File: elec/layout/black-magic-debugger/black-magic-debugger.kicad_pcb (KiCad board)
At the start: 2 copper layers, 24 parts

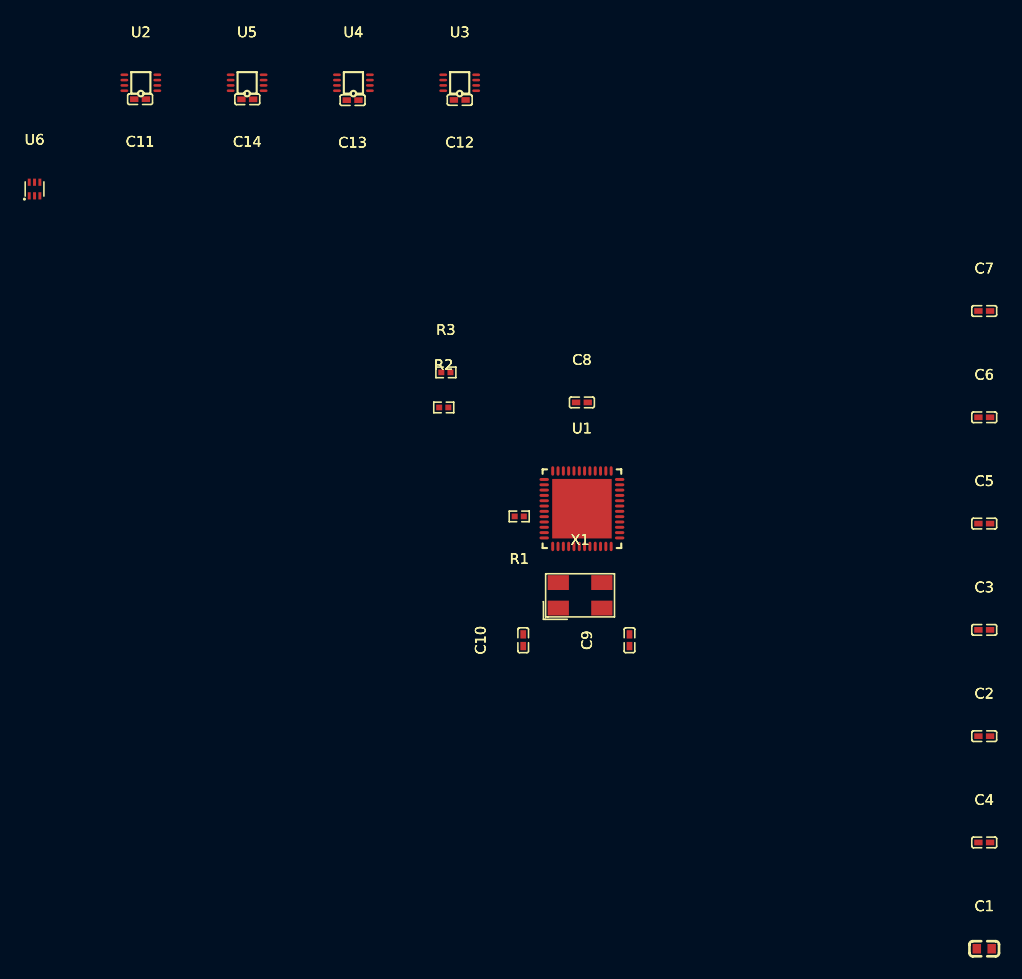
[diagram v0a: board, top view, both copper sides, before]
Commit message: add SWD header, finished routing
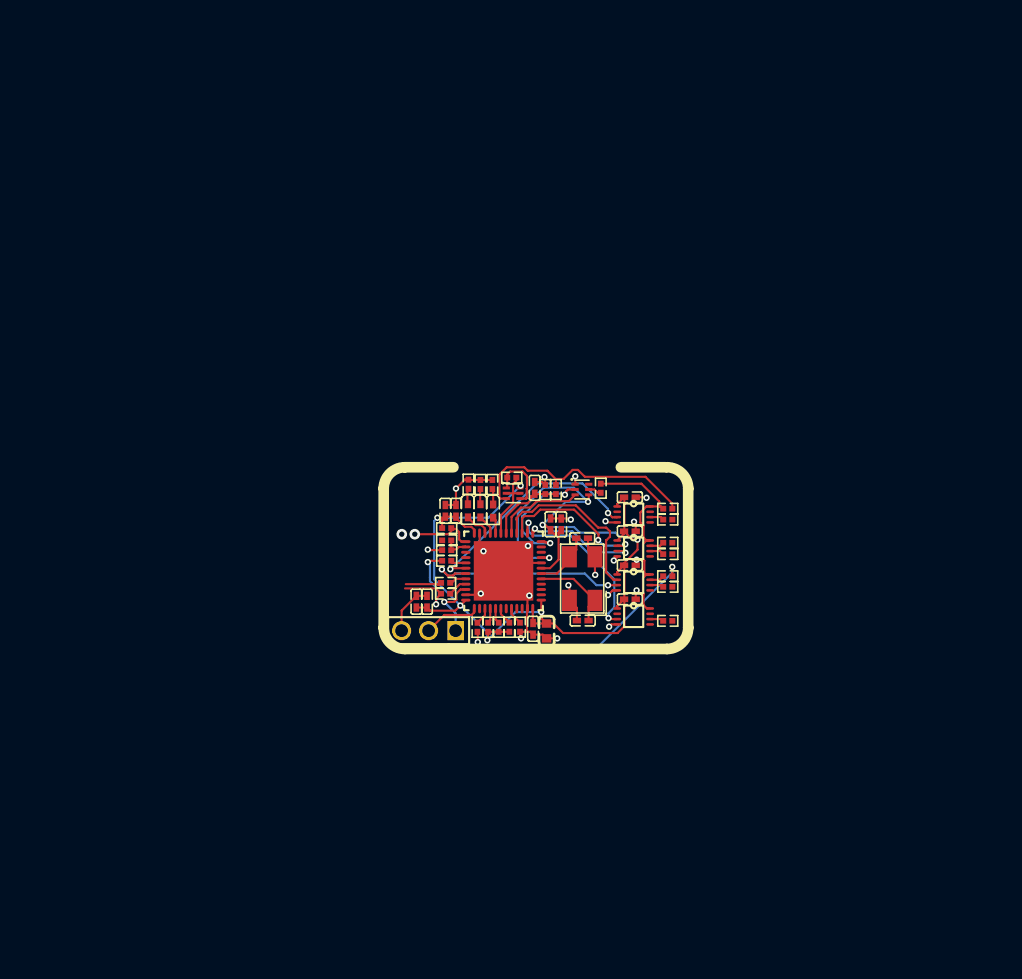
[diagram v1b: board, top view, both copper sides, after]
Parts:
- added C15: 100nF ±10% 16V X7R, atopile:C0402-b3ef17, F.Cu at (117.5, 51.4)
- added D1: , atopile:LED0402-R-RD-049f90, F.Cu at (113.6, 53.6)
- added D2: , atopile:LED0402-R-RD-049f90, F.Cu at (112.4, 53.6)
- added D3: , atopile:LED0402-R-RD-049f90, F.Cu at (111.2, 53.6)
- added P1: , atopile:HDR-TH_3P-P2.54-V-M-1-04b1f3, F.Cu at (107.5, 64.8)
- added R10: 1.5kΩ ±1% 62.5mW, atopile:R0402-56259e, F.Cu at (109.2, 58.3)
- added R11: 10kΩ ±1% 62.5mW, atopile:R0402-56259e, F.Cu at (109.2, 55.2)
- added R12: 10kΩ ±1% 62.5mW, atopile:R0402-56259e, F.Cu at (115.3, 50.5)
- added R13: 10kΩ ±1% 62.5mW, atopile:R0402-56259e, F.Cu at (123.7, 51.5)
- added R14: 100Ω ±1% 62.5mW, atopile:R0402-56259e, F.Cu at (130.0, 56.6)
- added R15: 100Ω ±1% 62.5mW, atopile:R0402-56259e, F.Cu at (130.0, 57.6)
- added R16: 100Ω ±1% 62.5mW, atopile:R0402-56259e, F.Cu at (130.0, 59.7)
- added R17: 100Ω ±1% 62.5mW, atopile:R0402-56259e, F.Cu at (130.0, 63.9)
- added R18: 100Ω ±1% 62.5mW, atopile:R0402-56259e, F.Cu at (112.1, 64.5)
- added R20: 10kΩ ±1% 62.5mW, atopile:R0402-56259e, F.Cu at (109.2, 57.3)
- added R21: 4.7kΩ ±1% 62.5mW, atopile:R0402-56259e, F.Cu at (109.2, 56.4)
- added R22: 10kΩ ±1% 62.5mW, atopile:R0402-56259e, F.Cu at (118.5, 51.6)
- added R23: 4.7kΩ ±1% 62.5mW, atopile:R0402-56259e, F.Cu at (119.5, 51.6)
- added R24: 100Ω ±1% 62.5mW, atopile:R0402-56259e, F.Cu at (130.0, 53.4)
- added R25: 100Ω ±1% 62.5mW, atopile:R0402-56259e, F.Cu at (130.0, 60.7)
- added R26: 100Ω ±1% 62.5mW, atopile:R0402-56259e, F.Cu at (130.0, 54.4)
- added R4: 10kΩ ±1% 62.5mW, atopile:R0402-56259e, F.Cu at (113.1, 64.5)
- added R5: 10kΩ ±1% 62.5mW, atopile:R0402-56259e, F.Cu at (114.1, 64.5)
- added R6: 10kΩ ±1% 62.5mW, atopile:R0402-56259e, F.Cu at (115.1, 64.5)
- added R7: 1kΩ ±1% 62.5mW, atopile:R0402-56259e, F.Cu at (113.5, 51.1)
- added R8: 1kΩ ±1% 62.5mW, atopile:R0402-56259e, F.Cu at (112.4, 51.1)
- added R9: 1kΩ ±1% 62.5mW, atopile:R0402-56259e, F.Cu at (111.3, 51.1)
- added U7: , atopile:SOT-563-6_L1.6-W1.2-P0.5-LS1.6-BL-d9216f, F.Cu at (121.9, 51.6)
- moved U5 62.0 mm to (126.8, 63.5), turned to 180 degrees
- moved U2 61.6 mm to (126.8, 53.9), turned to 180 degrees
- moved C11 59.4 mm to (126.5, 52.3), turned to 0 degrees
- moved C14 59.2 mm to (126.5, 61.9), turned to 0 degrees
- moved C4 57.1 mm to (107.4, 62.1), turned to 90 degrees
- moved C2 54.9 mm to (106.4, 62.1), turned to 90 degrees
- moved C7 54.1 mm to (109.1, 53.6), turned to 90 degrees
- moved U4 53.9 mm to (126.8, 60.3), turned to 180 degrees
- moved U6 53.4 mm to (115.5, 51.9), turned to -90 degrees
- moved C1 50.9 mm to (118.6, 64.9), turned to -90 degrees
- moved C5 49.7 mm to (110.1, 53.6), turned to 90 degrees
- moved C13 48.2 mm to (126.5, 55.5), turned to 0 degrees
- moved U3 46.8 mm to (126.8, 57.1), turned to 180 degrees
- moved C12 46.6 mm to (126.5, 58.7), turned to 0 degrees
- moved C3 42.5 mm to (117.3, 64.7), turned to -90 degrees
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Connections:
- net level_shifter_1-A1 renamed lvl_shifter_1-A1
- net level_shifter_1-B1 renamed lvl_shifter_1-B1
- net level_shifter_1-DIR renamed lvl_shifter_1-DIR
- net level_shifter_2-DIR renamed lvl_shifter_2-DIR
- net level_shifter_3-DIR renamed lvl_shifter_3-DIR
- net level_shifter_4-A1 renamed lvl_shifter_4-A1
- net level_shifter_4-B1 renamed lvl_shifter_4-B1
- net level_shifter_4-DIR renamed lvl_shifter_4-DIR
- C1 pad 1: hv-3 -> hv
- C10 pad 2: gnd-3 -> gnd
- C11 pad 1: hv-4 -> hv
- C11 pad 2: gnd-4 -> gnd
- C12 pad 1: hv-1 -> hv
- C12 pad 2: gnd-5 -> gnd
- C13 pad 1: hv-2 -> hv
- C13 pad 2: gnd-2 -> gnd
- C14 pad 2: gnd-1 -> gnd
- C2 pad 1: hv-3 -> hv
- C3 pad 1: hv-3 -> hv
- C4 pad 1: hv-3 -> hv
- C5 pad 1: hv-3 -> hv
- C6 pad 1: hv-3 -> hv
- C7 pad 1: hv-3 -> hv
- C9 pad 2: gnd-3 -> gnd
- U1 pad 1: hv-3 -> hv
- U1 pad 12: PA2 -> G2
- U1 pad 13: PA3 -> line-9
- U1 pad 14: PA4 -> line
- U1 pad 15: PA5 -> line-13
- U1 pad 16: PA6 -> line-7
- U1 pad 17: PA7 -> D1
- U1 pad 18: PB0 -> line-6
- U1 pad 19: PB1 -> G2-1
- U1 pad 20: PB2 -> anode
- U1 pad 21: PB10 -> anode-1
- U1 pad 22: PB11 -> anode-2
- U1 pad 24: hv-3 -> hv
- U1 pad 26: PB13 -> line-10
- U1 pad 30: PA9 -> line-12
- U1 pad 31: PA10 -> line-3
- U1 pad 36: hv-3 -> hv
- U1 pad 48: hv-3 -> hv
- U1 pad 49: EP -> gnd
- U1 pad 9: hv-3 -> hv
- U2 pad 1: hv-4 -> hv
- U2 pad 3: level_shifter_1-A2 -> line-12
- U2 pad 4: gnd-4 -> gnd
- U2 pad 6: level_shifter_1-B2 -> B2-2
- U2 pad 8: level_shifter_1-VCCB -> VCCB
- U3 pad 1: hv-1 -> hv
- U3 pad 2: level_shifter_2-A1 -> line-13
- U3 pad 3: level_shifter_2-A2 -> line-9
- U3 pad 4: gnd-5 -> gnd
- U3 pad 6: level_shifter_2-B2 -> B2
- U3 pad 7: level_shifter_2-B1 -> B1-1
- U3 pad 8: level_shifter_2-VCCB -> VCCB
- U4 pad 1: hv-2 -> hv
- U4 pad 2: level_shifter_3-A1 -> line-7
- U4 pad 3: level_shifter_3-A2 -> line-3
- U4 pad 4: gnd-2 -> gnd
- U4 pad 6: level_shifter_3-B2 -> B2-1
- U4 pad 7: level_shifter_3-B1 -> B1
- U4 pad 8: level_shifter_3-VCCB -> VCCB
- U5 pad 3: level_shifter_4-A2 -> line
- U5 pad 4: gnd-1 -> gnd
- U5 pad 6: level_shifter_4-B2 -> B2-3
- U5 pad 8: level_shifter_4-VCCB -> VCCB
- U6 pad 1: S2 -> S1
- U6 pad 2: G2 -> G2-1
- U6 pad 3: D1 -> hv-2
- U6 pad 5: G1 -> G2-1
- U6 pad 6: D2 -> hv
- X1 pad 2: gnd-3 -> gnd
- X1 pad 4: gnd-3 -> gnd
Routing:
- net hv: track 0.00 -> 106.5 mm, vias 0 -> 9
- net gnd: track 0.00 -> 61.6 mm, vias 0 -> 22
- net line-1: track 0.00 -> 23.7 mm, vias 0 -> 2
- net hv-2: track 0.00 -> 22.7 mm
- net line-12: track 0.00 -> 22.2 mm, vias 0 -> 2
- net VCCB: track 0.00 -> 20.7 mm
- net line-3: track 0.00 -> 19.9 mm, vias 0 -> 2
- net line-7: track 0.00 -> 17.1 mm
- net line: track 0.00 -> 16.5 mm, vias 0 -> 2
- net line-13: track 0.00 -> 14.1 mm, vias 0 -> 2
- net G2: track 0.00 -> 11.6 mm, vias 0 -> 2
- net line-9: track 0.00 -> 10.8 mm, vias 0 -> 2
- net micro-line-1: track 0.00 -> 10.5 mm, vias 0 -> 2
- net D1: track 0.00 -> 8.37 mm
- net xin: track 0.00 -> 8.04 mm
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
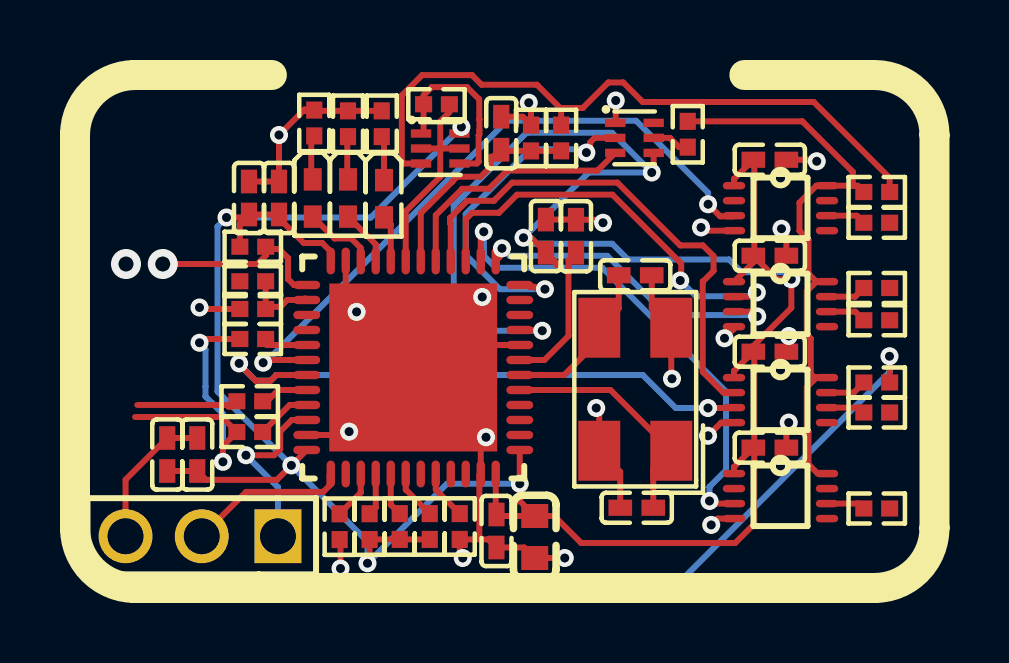
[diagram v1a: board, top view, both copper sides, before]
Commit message: Correct DIR pins
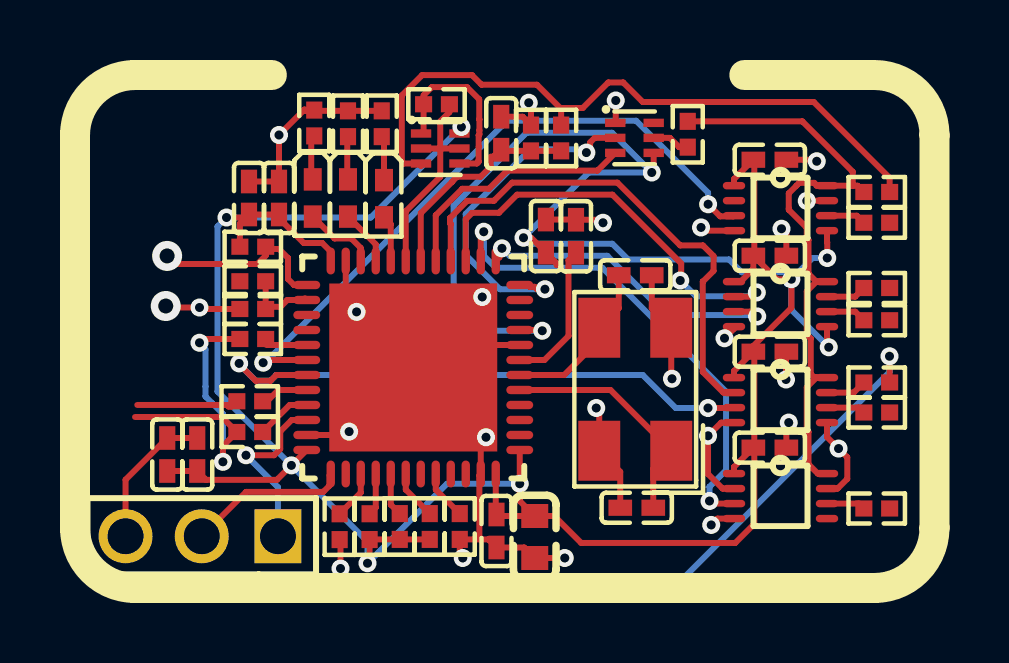
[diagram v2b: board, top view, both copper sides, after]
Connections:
- net lvl_shifter_4-DIR renamed DIR
- C15 pad 1: line-6 -> line-5
- R10 pad 1: micro-line-1 -> line-4
- R12 pad 1: G2-1 -> G1
- R13 pad 2: G1 -> G1-1
- R14 pad 2: line-2 -> line-13
- R15 pad 2: line-11 -> line-3
- R16 pad 2: line-1 -> line-2
- R17 pad 1: B2-3 -> B2-2
- R17 pad 2: line-4 -> line
- R18 pad 2: line-1 -> line-2
- R2 pad 1: micro-line -> line-9
- R20 pad 1: line-10 -> line-11
- R21 pad 1: hv-1 -> hv-2
- R21 pad 2: line-10 -> line-11
- R22 pad 1: line-6 -> line-5
- R23 pad 1: hv-2 -> hv-1
- R23 pad 2: line-6 -> line-5
- R24 pad 2: hv-2 -> hv-1
- R25 pad 1: B2-1 -> B2-3
- R25 pad 2: line-8 -> line-15
- R26 pad 1: B2-2 -> B2-1
- R26 pad 2: line-5 -> line-6
- R3 pad 1: micro-line-1 -> line-4
- U1 pad 13: line-9 -> line-1
- U1 pad 14: line -> line-7
- U1 pad 15: line-13 -> line-14
- U1 pad 16: line-7 -> line-12
- U1 pad 18: line-6 -> line-5
- U1 pad 19: G2-1 -> G1
- U1 pad 26: line-10 -> line-11
- U1 pad 30: line-12 -> line-10
- U1 pad 31: line-3 -> line-8
- U2 pad 2: lvl_shifter_1-A1 -> gnd
- U2 pad 3: line-12 -> line-10
- U2 pad 5: lvl_shifter_1-DIR -> hv
- U2 pad 6: B2-2 -> B2-1
- U2 pad 7: lvl_shifter_1-B1 -> gnd
- U3 pad 2: line-13 -> line-14
- U3 pad 3: line-9 -> line-1
- U3 pad 5: lvl_shifter_2-DIR -> hv
- U4 pad 2: line-7 -> line-12
- U4 pad 3: line-3 -> line-8
- U4 pad 5: lvl_shifter_3-DIR -> gnd
- U4 pad 6: B2-1 -> B2-3
- U5 pad 2: lvl_shifter_4-A1 -> gnd
- U5 pad 3: line -> line-7
- U5 pad 6: B2-3 -> B2-2
- U5 pad 7: lvl_shifter_4-B1 -> gnd
- U6 pad 2: G2-1 -> G1
- U6 pad 3: hv-2 -> hv-1
- U6 pad 5: G2-1 -> G1
- U7 pad 5: G1 -> G1-1
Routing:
- net line-2: track 0.00 -> 23.7 mm, vias 0 -> 2
- net hv-2: track 22.7 -> 0.00 mm
- net hv-1: track 0.00 -> 22.7 mm
- net line-8: track 0.00 -> 19.9 mm, vias 0 -> 2
- net line-3: track 19.9 -> 0.00 mm, vias 2 -> 0
- net line-10: track 2.58 -> 22.2 mm, vias 0 -> 2
- net line: track 16.5 -> 0.00 mm, vias 2 -> 0
- net line-14: track 0.00 -> 14.1 mm, vias 0 -> 2
- net line-13: track 14.1 -> 0.00 mm, vias 2 -> 0
- net line-1: track 23.7 -> 10.8 mm
- net micro-line-1: track 10.5 -> 0.00 mm, vias 2 -> 0
- net line-4: track 0.00 -> 10.5 mm, vias 0 -> 2
- net gnd: track 61.6 -> 69.1 mm, vias 22 -> 24
- net line-9: track 10.8 -> 3.41 mm, vias 2 -> 0
- net line-6: track 7.33 -> 0.00 mm
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
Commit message: Build everything with ordered params to fix frozen builds
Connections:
- net S1 renamed S2
- C1 pad 1: hv -> hv-2
- C11 pad 1: hv -> hv-2
- C12 pad 1: hv -> hv-2
- C13 pad 1: hv -> hv-2
- C14 pad 1: hv -> hv-2
- C15 pad 1: line-5 -> line-12
- C2 pad 1: hv -> hv-2
- C3 pad 1: hv -> hv-2
- C4 pad 1: hv -> hv-2
- C5 pad 1: hv -> hv-2
- C6 pad 1: hv -> hv-2
- C7 pad 1: hv -> hv-2
- D1 pad 1: anode -> anode-2
- D3 pad 1: anode-2 -> anode
- R10 pad 1: line-4 -> line-6
- R11 pad 2: hv -> hv-2
- R12 pad 1: G1 -> G1-1
- R13 pad 2: G1-1 -> G1
- R14 pad 2: line-13 -> line-4
- R15 pad 1: B2 -> B2-1
- R15 pad 2: line-3 -> line-13
- R16 pad 2: line-2 -> line-7
- R17 pad 2: line -> line-11
- R18 pad 2: line-2 -> line-7
- R2 pad 1: line-9 -> line-15
- R20 pad 1: line-11 -> line-1
- R21 pad 1: hv-2 -> hv-1
- R21 pad 2: line-11 -> line-1
- R22 pad 1: line-5 -> line-12
- R23 pad 1: hv-1 -> hv
- R23 pad 2: line-5 -> line-12
- R24 pad 2: hv-1 -> hv
- R25 pad 1: B2-3 -> B2
- R25 pad 2: line-15 -> line-3
- R26 pad 1: B2-1 -> B2-3
- R26 pad 2: line-6 -> line-8
- R3 pad 1: line-4 -> line-6
- R4 pad 2: hv -> hv-2
- R5 pad 2: hv -> hv-2
- R6 pad 2: hv -> hv-2
- U1 pad 1: hv -> hv-2
- U1 pad 11: PA1 -> DIR
- U1 pad 13: line-1 -> line
- U1 pad 14: line-7 -> line-5
- U1 pad 16: line-12 -> line-9
- U1 pad 18: line-5 -> line-12
- U1 pad 19: G1 -> G1-1
- U1 pad 20: anode -> anode-2
- U1 pad 22: anode-2 -> anode
- U1 pad 24: hv -> hv-2
- U1 pad 26: line-11 -> line-1
- U1 pad 30: line-10 -> line-2
- U1 pad 31: line-8 -> line-10
- U1 pad 36: hv -> hv-2
- U1 pad 48: hv -> hv-2
- U1 pad 9: hv -> hv-2
- U2 pad 1: hv -> hv-2
- U2 pad 3: line-10 -> line-2
- U2 pad 5: hv -> hv-2
- U2 pad 6: B2-1 -> B2-3
- U3 pad 1: hv -> hv-2
- U3 pad 3: line-1 -> line
- U3 pad 5: hv -> hv-2
- U3 pad 6: B2 -> B2-1
- U4 pad 1: hv -> hv-2
- U4 pad 2: line-12 -> line-9
- U4 pad 3: line-8 -> line-10
- U4 pad 6: B2-3 -> B2
- U5 pad 1: hv -> hv-2
- U5 pad 3: line-7 -> line-5
- U6 pad 2: G1 -> G1-1
- U6 pad 3: hv-1 -> hv
- U6 pad 5: G1 -> G1-1
- U6 pad 6: hv -> hv-2
- U7 pad 4: hv -> hv-2
- U7 pad 5: G1-1 -> G1
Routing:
- net hv-2: track 0.00 -> 112.6 mm, vias 0 -> 11
- net hv: track 112.6 -> 22.7 mm, vias 11 -> 0
- net hv-1: track 22.7 -> 0.00 mm
- net line-8: track 19.9 -> 0.00 mm, vias 2 -> 0
- net line-9: track 3.41 -> 17.1 mm
- net line: track 0.00 -> 10.8 mm, vias 0 -> 2
- net line-6: track 0.00 -> 10.5 mm, vias 0 -> 2
- net line-4: track 10.5 -> 0.00 mm, vias 2 -> 0
- net line-12: track 17.1 -> 7.33 mm
- net line-5: track 7.33 -> 16.5 mm, vias 0 -> 2
- net line-1: track 10.8 -> 2.58 mm, vias 2 -> 0
- net line-7: track 16.5 -> 23.7 mm
- net G1-1: track 1.26 -> 7.11 mm
- net G1: track 7.11 -> 1.26 mm
- net line-15: track 0.00 -> 3.41 mm
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
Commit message: checkin
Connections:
- C1 pad 1: hv-2 -> hv-1
- C11 pad 1: hv-2 -> hv-1
- C12 pad 1: hv-2 -> hv-1
- C13 pad 1: hv-2 -> hv-1
- C14 pad 1: hv-2 -> hv-1
- C15 pad 1: line-12 -> line
- C2 pad 1: hv-2 -> hv-1
- C3 pad 1: hv-2 -> hv-1
- C4 pad 1: hv-2 -> hv-1
- C5 pad 1: hv-2 -> hv-1
- C6 pad 1: hv-2 -> hv-1
- C7 pad 1: hv-2 -> hv-1
- D1 pad 1: anode-2 -> anode-1
- D2 pad 1: anode-1 -> anode
- D3 pad 1: anode -> anode-2
- R10 pad 1: line-6 -> line-14
- R11 pad 2: hv-2 -> hv-1
- R12 pad 1: G1-1 -> G1
- R13 pad 2: G1 -> G1-1
- R14 pad 2: line-4 -> line-10
- R15 pad 1: B2-1 -> B2
- R15 pad 2: line-13 -> line-5
- R16 pad 2: line-7 -> line-13
- R17 pad 1: B2-2 -> B2-3
- R17 pad 2: line-11 -> line-1
- R18 pad 2: line-7 -> line-13
- R2 pad 1: line-15 -> line-9
- R20 pad 1: line-1 -> line-6
- R21 pad 1: hv-1 -> hv
- R21 pad 2: line-1 -> line-6
- R22 pad 1: line-12 -> line
- R23 pad 1: hv -> hv-2
- R23 pad 2: line-12 -> line
- R24 pad 2: hv -> hv-2
- R25 pad 1: B2 -> B2-2
- R25 pad 2: line-3 -> line-4
- R26 pad 1: B2-3 -> B2-1
- R26 pad 2: line-8 -> line-15
- R3 pad 1: line-6 -> line-14
- R4 pad 2: hv-2 -> hv-1
- R5 pad 2: hv-2 -> hv-1
- R6 pad 2: hv-2 -> hv-1
- U1 pad 1: hv-2 -> hv-1
- U1 pad 13: line -> line-2
- U1 pad 14: line-5 -> line-11
- U1 pad 15: line-14 -> line-12
- U1 pad 16: line-9 -> line-8
- U1 pad 18: line-12 -> line
- U1 pad 19: G1-1 -> G1
- U1 pad 20: anode-2 -> anode-1
- U1 pad 21: anode-1 -> anode
- U1 pad 22: anode -> anode-2
- U1 pad 24: hv-2 -> hv-1
- U1 pad 26: line-1 -> line-6
- U1 pad 30: line-2 -> line-3
- U1 pad 31: line-10 -> line-7
- U1 pad 36: hv-2 -> hv-1
- U1 pad 48: hv-2 -> hv-1
- U1 pad 9: hv-2 -> hv-1
- U2 pad 1: hv-2 -> hv-1
- U2 pad 3: line-2 -> line-3
- U2 pad 5: hv-2 -> hv-1
- U2 pad 6: B2-3 -> B2-1
- U3 pad 1: hv-2 -> hv-1
- U3 pad 2: line-14 -> line-12
- U3 pad 3: line -> line-2
- U3 pad 5: hv-2 -> hv-1
- U3 pad 6: B2-1 -> B2
- U4 pad 1: hv-2 -> hv-1
- U4 pad 2: line-9 -> line-8
- U4 pad 3: line-10 -> line-7
- U4 pad 6: B2 -> B2-2
- U5 pad 1: hv-2 -> hv-1
- U5 pad 3: line-5 -> line-11
- U5 pad 6: B2-2 -> B2-3
- U6 pad 2: G1-1 -> G1
- U6 pad 3: hv -> hv-2
- U6 pad 5: G1-1 -> G1
- U6 pad 6: hv-2 -> hv-1
- U7 pad 4: hv-2 -> hv-1
- U7 pad 5: G1 -> G1-1
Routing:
- net hv-1: track 0.00 -> 112.6 mm, vias 0 -> 11
- net hv-2: track 112.6 -> 22.7 mm, vias 11 -> 0
- net line-13: track 0.00 -> 23.7 mm, vias 0 -> 2
- net hv: track 22.7 -> 0.00 mm
- net line-3: track 0.00 -> 22.2 mm, vias 0 -> 2
- net line-10: track 19.9 -> 0.00 mm, vias 2 -> 0
- net line-8: track 0.00 -> 17.1 mm
- net line-5: track 16.5 -> 0.00 mm, vias 2 -> 0
- net line-11: track 0.00 -> 16.5 mm, vias 0 -> 2
- net line-9: track 17.1 -> 3.41 mm
- net line-2: track 22.2 -> 10.8 mm
- net line-6: track 10.5 -> 2.58 mm, vias 2 -> 0
- net line-12: track 7.33 -> 14.1 mm, vias 0 -> 2
- net G1-1: track 7.11 -> 1.26 mm
- net G1: track 1.26 -> 7.11 mm
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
